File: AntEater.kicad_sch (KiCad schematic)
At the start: 3 parts, among them CN1 X2026WRS-2X09D-LPSW, CN2 X2026WRS-2X09D-LPSW, J1 Conn_01x10_MountingPin

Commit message: placed and routed
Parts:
- removed J1: Conn_01x10_MountingPin, Connector_PinHeader_2.54mm:PinHeader_1x11_P2.54mm_Vertical, symbol Connector_Generic:Conn_01x11
- added C1, C11, C12, C13, C14, C3, C5, C8, C9: 0.1uF, Capacitor_SMD:C_0805_2012Metric, symbol Device:C
- added C10: 3.3uF, Capacitor_SMD:C_0805_2012Metric, symbol Device:C
- added C2, C7: 27pf, Capacitor_SMD:C_0805_2012Metric, symbol Device:C
- added C4, C6: 4.7uF, Capacitor_SMD:C_1206_3216Metric, symbol Device:C_Polarized
- added FB1, FB2: FerriteBead_Small, Resistor_SMD:R_0603_1608Metric, symbol Device:FerriteBead_Small
- added J2: USB_C_Receptacle_USB2.0, Connector_USB:USB_C_Receptacle_GCT_USB4105-xx-A_16P_TopMnt_Horizontal, symbol Connector:USB_C_Receptacle_USB2.0
- added J3: Conn_02x06_Odd_Even, Connector_PinHeader_2.54mm:PinHeader_2x06_P2.54mm_Vertical, symbol Connector_Generic:Conn_02x06_Odd_Even
- added JP1, JP2: SolderJumper_2_Open, Jumper:SolderJumper-2_P1.3mm_Open_RoundedPad1.0x1.5mm, symbol Jumper:SolderJumper_2_Open
- added R1: 2.2K, Resistor_SMD:R_0805_2012Metric, symbol Device:R_US
- added R2, R3, R4: 10K, Resistor_SMD:R_0805_2012Metric, symbol Device:R_US
- added R5, R7: 5.1K, Resistor_SMD:R_0805_2012Metric, symbol Device:R_US
- added R6: 12K, Resistor_SMD:R_0805_2012Metric, symbol Device:R_US
- added R8: 1K, Resistor_SMD:R_0805_2012Metric, symbol Device:R_US
- added U1: M93C46-WDW6TP, bitcrane:TSSOP8_STM, symbol bitcrane:M93C46-WDW6TP
- added U2: FT4232HQ, bitcrane:QFN50P900X900X105-65N, symbol bitcrane:FT4232HQ-REEL
- added Y1: 12MHz, bitcrane:XTAL_405C35B12M00000, symbol bitcrane:405C35B12M00000
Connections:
- net A0: now also J3.10 (Pin_10)
- net A1: now also J3.5 (Pin_5)
- net A2: now also J3.1 (Pin_1)
- net GND: now also C1.2, C10.2, C11.2, C12.2, C13.2, C14.2, C2.2, C3.2, C4.2, C5.2, C6.2, C7.2, C8.2, C9.2, J2.A1 (GND), J2.A12 (GND), J2.B1 (GND), J2.B12 (GND), J2.S1 (SHIELD), J3.11 (Pin_11), J3.12 (Pin_12), R5.1, R6.1, R7.1, U1.5 (VSS), U1.7 (DU), U2.1 (GND), U2.10 (AGND), U2.11 (GND), U2.13 (TEST), U2.15 (GND), U2.25 (GND), U2.35 (GND), U2.47 (GND), U2.5 (GND), U2.51 (GND), U2.65 (EPAD), Y1.2 (GND), Y1.4 (GND__1)
- net PLUG: now also J3.4 (Pin_4)
- net RST: now also J3.7 (Pin_7)
- net RX: now also J3.9 (Pin_9), JP2.2 (B), U2.39 (CDBUS1)
- net SCL: now also J3.2 (Pin_2), U2.16 (ADBUS0)
- net SDA: now also J3.3 (Pin_3), U2.17 (ADBUS1), U2.18 (ADBUS2)
- net TX: now also J3.6 (Pin_6), JP1.2 (B), U2.27 (BDBUS1)
- net 3V3 renamed VCCIO
- net VCCIO: now also C11.1, C13.1, C14.1, C8.1, FB1.1, FB2.1, J3.8 (Pin_8), R2.2, R3.2, R4.2, R8.1, U1.6 (ORG), U1.8 (VCC), U2.20 (VCCIO), U2.31 (VCCIO), U2.42 (VCCIO), U2.50 (VREGIN), U2.56 (VCCIO)
- new net: C12.1, C4.1, FB1.2, U2.4 (VPHY)
- new net: JP2.1 (A), U2.26 (BDBUS0)
- new net: R1.1, U1.3 (D), U2.61 (EEDATA)
- new net: R1.2, R2.1, U1.4 (Q)
- new net: C2.1, U2.2 (OSCI), Y1.1
- new net: C7.1, U2.3 (OSCO), Y1.3
- new net: R4.1, U1.2 (CLK), U2.62 (EECLK)
- new net: C6.1, C9.1, FB2.2, U2.9 (VPLL)
- new net: R3.1, U1.1 (CS), U2.63 (EECS)
- new net: R8.2, U2.14 (RESET#)
- new net: JP1.1 (A), U2.38 (CDBUS0)
- new net: R6.2, U2.6 (REF)
- new net: J2.A7 (D-), J2.B7 (D-), U2.7 (DM)
- new net: J2.A6 (D+), J2.B6 (D+), U2.8 (DP)
- new net: J2.A5 (CC1), R7.2
- new net: J2.B5 (CC2), R5.2
- new net 5V: J2.A4 (VBUS), J2.A9 (VBUS), J2.B4 (VBUS), J2.B9 (VBUS)
- new net VCORE: C1.1, C10.1, C3.1, C5.1, U2.12 (VCORE), U2.37 (VCORE), U2.49 (VREGOUT), U2.64 (VCORE)
- no-connect marks 4 -> 33
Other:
- note added: "RXD"
- note added: "TXD"
- moved on the sheet: CN2

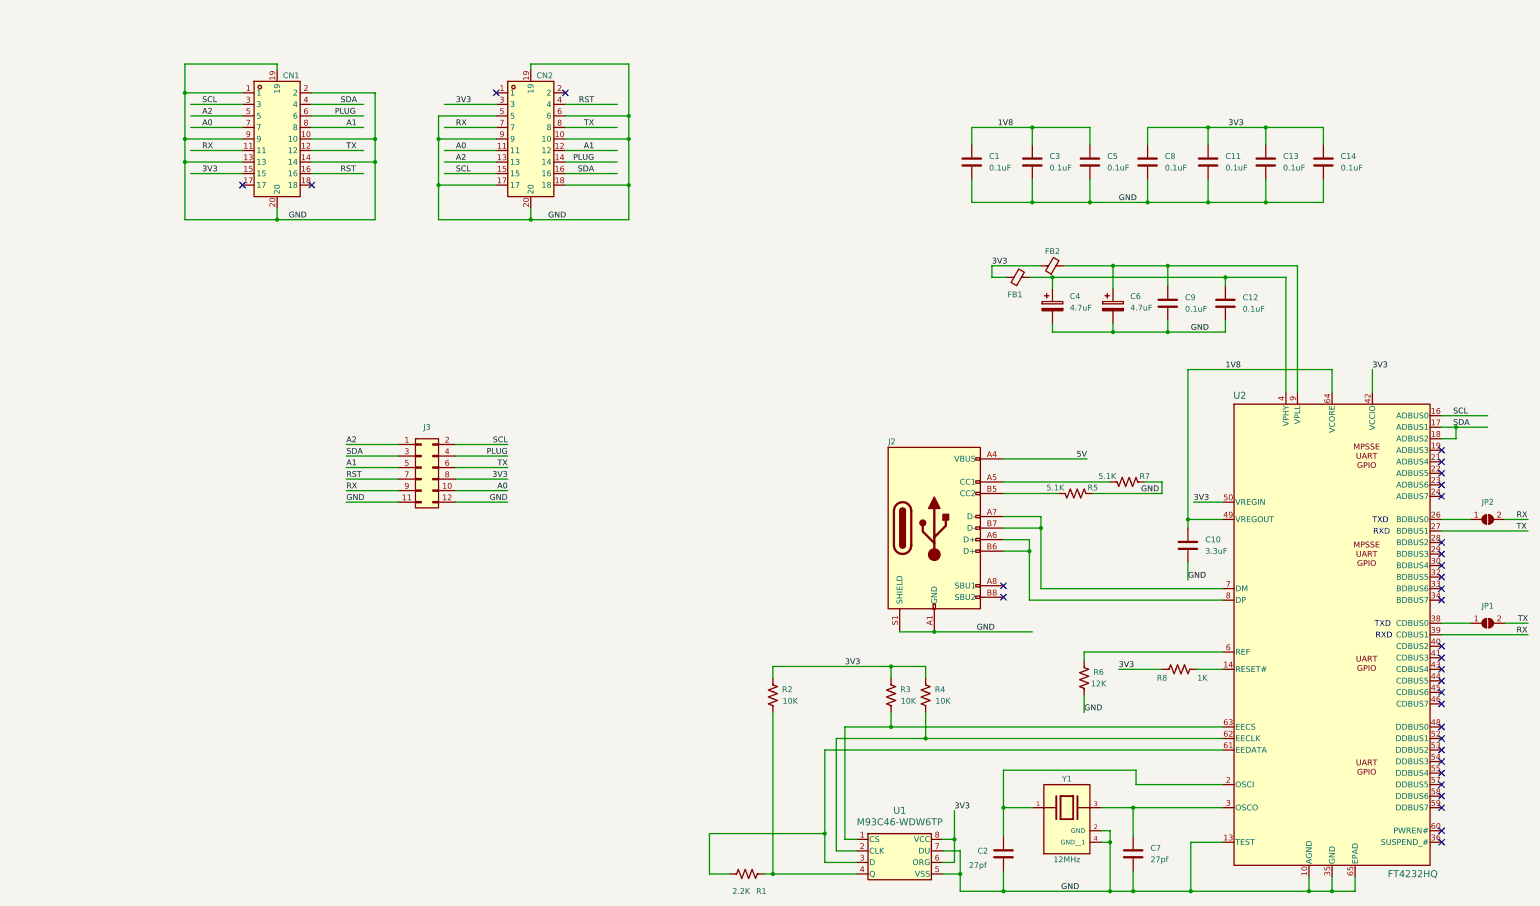
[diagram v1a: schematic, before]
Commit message: added an optional voltage regulator. DRC passed. generated gerbers
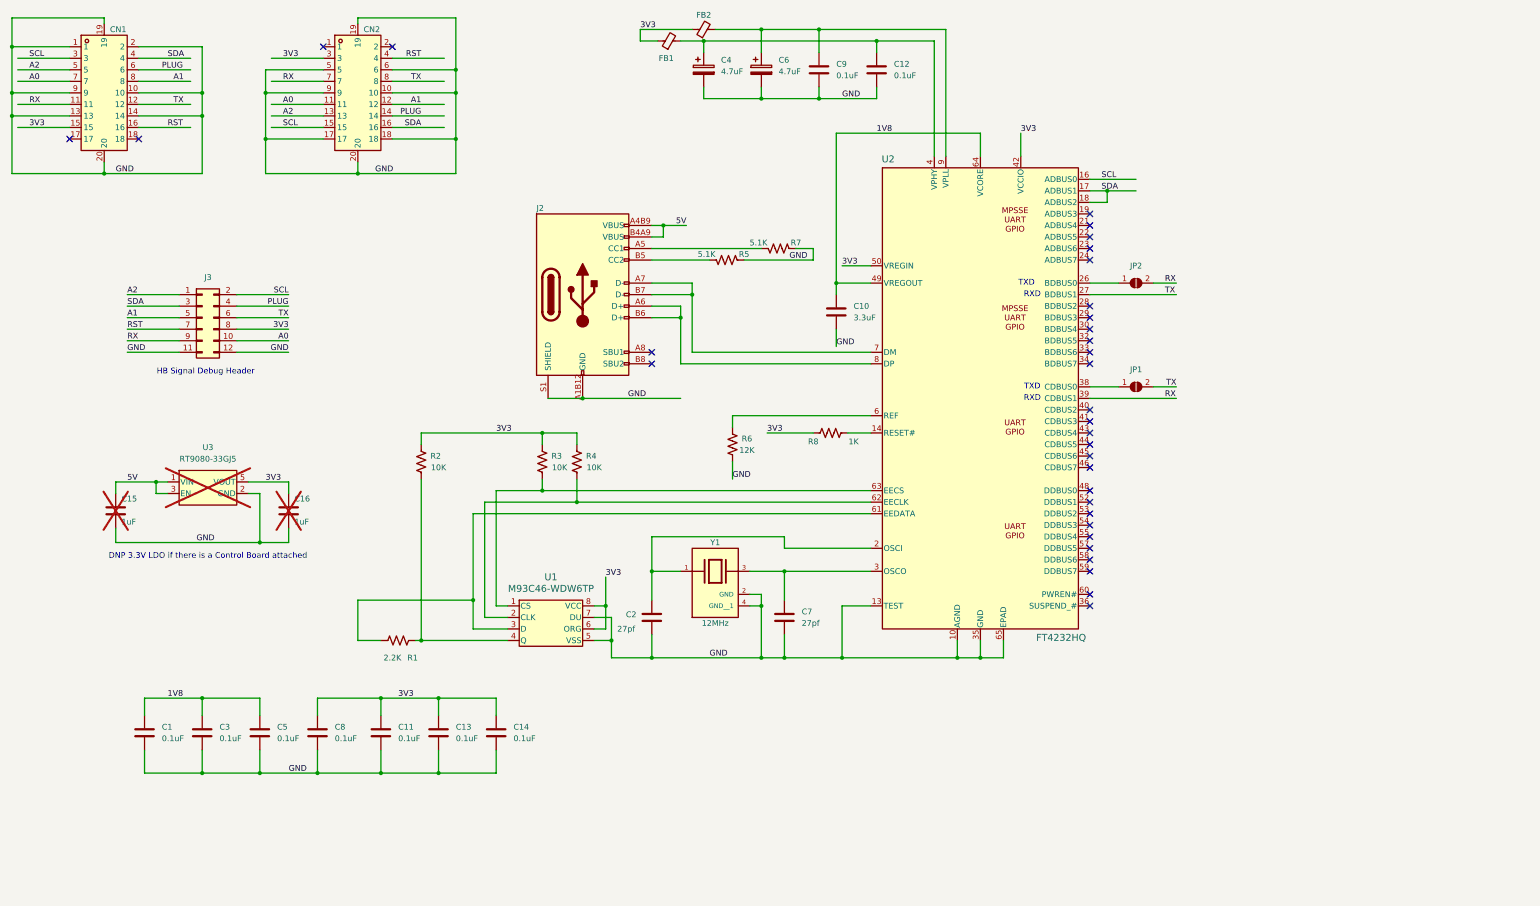
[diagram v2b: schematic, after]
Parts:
- removed J2: USB_C_Receptacle_USB2.0, Connector_USB:USB_C_Receptacle_GCT_USB4105-xx-A_16P_TopMnt_Horizontal, symbol Connector:USB_C_Receptacle_USB2.0
- added C15, C16: 1uF, Capacitor_SMD:C_0805_2012Metric, symbol Device:C
- added J2: USB_C_Receptacle_USB2.0, antsniffer:USB_C_Receptacle_GCT_USB4105-xx-A_16P_TopMnt_Horizontal, symbol antsniffer:USB_C_Receptacle_USB2.0
- added U3: RT9080-33GJ5, antsniffer:RT9080-33GJ5, symbol antsniffer:RT9080-33GJ5
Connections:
- net 5V: now also C15.1, J2.A4B9 (VBUS), J2.B4A9 (VBUS), U3.1 (VIN), U3.3 (EN)
- net GND: now also C15.2, C16.2, J2.A1B12 (GND), J2.B1A12 (GND), J2.S1 (SHIELD), U3.2 (GND)
- net VCCIO: now also C16.1, U3.5 (VOUT)
- net at U2.7 (DM): now also J2.A7 (D-), J2.B7 (D-)
- net at U2.8 (DP): now also J2.A6 (D+), J2.B6 (D+)
- net at R7.2: now also J2.A5 (CC1)
- net at R5.2: now also J2.B5 (CC2)
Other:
- note added: "DNP 3.3V LDO if there is a Control Board attached"
- note added: "HB Signal Debug Header"
- moved on the sheet: C1, C10, C11, C12, C13, C14, C2, C3, C4, C5, C6, C7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

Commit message: switched schematic to RP2040
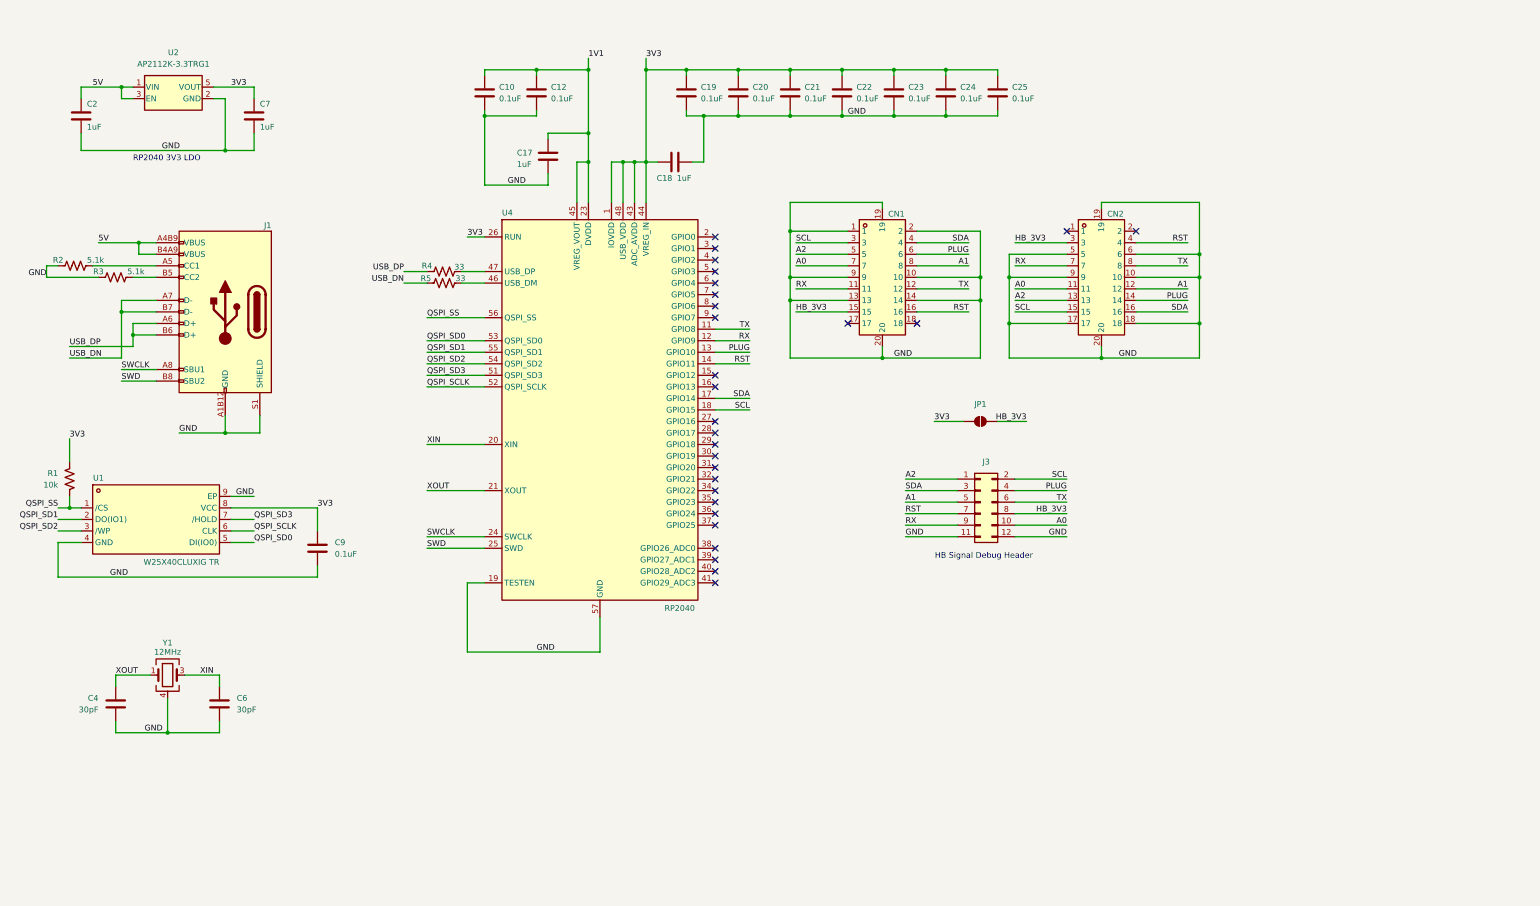
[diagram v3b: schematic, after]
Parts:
- removed C1, C11, C13, C14, C3, C5, C8: 0.1uF, Capacitor_SMD:C_0805_2012Metric, symbol Device:C
- removed C15, C16: 1uF, Capacitor_SMD:C_0805_2012Metric, symbol Device:C
- removed C4, C6: 4.7uF, Capacitor_SMD:C_1206_3216Metric, symbol Device:C_Polarized
- removed FB1, FB2: FerriteBead_Small, Resistor_SMD:R_0603_1608Metric, symbol Device:FerriteBead_Small
- removed J2: USB_C_Receptacle_USB2.0, antsniffer:USB_C_Receptacle_GCT_USB4105-xx-A_16P_TopMnt_Horizontal, symbol antsniffer:USB_C_Receptacle_USB2.0
- removed JP2: SolderJumper_2_Open, Jumper:SolderJumper-2_P1.3mm_Open_RoundedPad1.0x1.5mm, symbol Jumper:SolderJumper_2_Open
- removed R6: 12K, Resistor_SMD:R_0805_2012Metric, symbol Device:R_US
- removed R7: 5.1K, Resistor_SMD:R_0805_2012Metric, symbol Device:R_US
- removed R8: 1K, Resistor_SMD:R_0805_2012Metric, symbol Device:R_US
- removed U1: M93C46-WDW6TP, bitcrane:TSSOP8_STM, symbol bitcrane:M93C46-WDW6TP
- removed U2: FT4232HQ, bitcrane:QFN50P900X900X105-65N, symbol bitcrane:FT4232HQ-REEL
- removed U3: RT9080-33GJ5, antsniffer:RT9080-33GJ5, symbol antsniffer:RT9080-33GJ5
- removed Y1: 12MHz, bitcrane:XTAL_405C35B12M00000, symbol bitcrane:405C35B12M00000
- added C17, C18: 1uF, Capacitor_SMD:C_0402_1005Metric, symbol Device:C
- added C19, C20, C21, C22, C23, C24, C25: 0.1uF, Capacitor_SMD:C_0402_1005Metric, symbol Device:C
- added C4, C6: 30pF, Capacitor_SMD:C_0402_1005Metric, symbol Device:C
- added J1: USB_C_Receptacle_USB2.0, antsniffer:USB_C_Receptacle_GCT_USB4105-xx-A_16P_TopMnt_Horizontal, symbol antsniffer:USB_C_Receptacle_USB2.0
- added U1: W25X40CLUXIG TR, antsniffer:USON8_L2.0-W3.0-P0.50-BL-EP, symbol antsniffer:W25X40CLUXIGTR
- added U2: AP2112K-3.3TRG1, antsniffer:SOT-25-5_L2.9-W1.6-P0.95-LS2.8-BL, symbol antsniffer:AP2112K-3.3TRG1
- added U4: RP2040, Package_DFN_QFN:QFN-56-1EP_7x7mm_P0.4mm_EP3.2x3.2mm, symbol aditBoard:RP2040
- added Y1: 12MHz, antsniffer:OSC-SMD_4P-L3.2-W2.5-BL, symbol Device:Crystal_GND24_common
- C10: value 3.3uF -> 0.1uF; footprint Capacitor_SMD:C_0805_2012Metric -> Capacitor_SMD:C_0402_1005Metric; DK 1276-2912-1-ND -> (none); JLC Part (none) -> Basic Part; LCSC Part (none) -> C307331; Manufacturer (none) -> SAMSUNG(三星); PARTNO CL21A335KPFNNNE -> CL05B104KB54PNC
- C12, C9: footprint Capacitor_SMD:C_0805_2012Metric -> Capacitor_SMD:C_0402_1005Metric; DK 1276-6840-1-ND -> (none); JLC Part (none) -> Basic Part; LCSC Part (none) -> C307331; Manufacturer (none) -> SAMSUNG(三星); PARTNO CL21B104KCFNNNE -> CL05B104KB54PNC
- C2, C7: value 27pf -> 1uF; footprint Capacitor_SMD:C_0805_2012Metric -> Capacitor_SMD:C_0402_1005Metric; DK 1276-2622-1-ND -> 587-5514-1-ND; LCSC Part (none) -> C52923; PARTNO CL21C270JCANNNC -> EMK105BJ105MV-F
- R1: value 2.2K -> 10k; footprint Resistor_SMD:R_0805_2012Metric -> Resistor_SMD:R_0402_1005Metric; DK RMCF0805FT2K20CT-ND -> (none); LCSC Part (none) -> C25744; PARTNO RMCF0805FT2K20 -> (none)
- R2, R3: value 10K -> 5.1k; footprint Resistor_SMD:R_0805_2012Metric -> Resistor_SMD:R_0402_1005Metric; DK RMCF0805FT10K0CT-ND -> RMCF0402JT5K10CT-ND; LCSC Part (none) -> C25905; PARTNO RMCF0805FT10K0 -> RMCF0402JT5K10
- R4: value 10K -> 33; footprint Resistor_SMD:R_0805_2012Metric -> Resistor_SMD:R_0402_1005Metric; DK RMCF0805FT10K0CT-ND -> (none); JLC Part (none) -> Basic Part; LCSC Part (none) -> C25105; Manufacturer (none) -> UNI-ROYAL(厚声); PARTNO RMCF0805FT10K0 -> 0402WGF330JTCE
- R5: value 5.1K -> 33; footprint Resistor_SMD:R_0805_2012Metric -> Resistor_SMD:R_0402_1005Metric; DK 311-5.10KCRCT-ND -> (none); JLC Part (none) -> Basic Part; LCSC Part (none) -> C25105; Manufacturer (none) -> UNI-ROYAL(厚声); PARTNO RC0805FR-075K1L -> 0402WGF330JTCE
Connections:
- net VCORE is gone; now on net GND: C10.1
- net 5V: now also C2.1, J1.A4B9 (VBUS), J1.B4A9 (VBUS), U2.1 (VIN), U2.3 (EN)
- net GND: now also C12.1, C9.1, R2.1, R3.1, C17.1, C18.2, C19.1, C20.1, C21.1, C22.1, C23.1, C24.1, C25.1, C4.1, C6.1, J1.A1B12 (GND), J1.B1A12 (GND), J1.S1 (SHIELD), U1.4 (GND), U1.9 (EP), U2.2 (GND), U4.19 (TESTEN), U4.57 (GND), Y1.2, Y1.4; no longer C10.2, C12.2, C9.2, R5.1
- net PLUG: now also U4.13 (GPIO10)
- net RST: now also U4.14 (GPIO11)
- net RX: now also U4.12 (GPIO9)
- net SCL: now also U4.18 (GPIO15)
- net SDA: now also U4.17 (GPIO14)
- net TX: now also U4.11 (GPIO8); no longer JP1.2 (B)
- net at R5.2: now also U4.46 (USB_DM)
- net 3V3: now reaches R1.1
- net 3V3: now also C7.1, C9.2, JP1.1 (A), C18.1, C19.2, C20.2, C21.2, C22.2, C23.2, C24.2, C25.2, U1.8 (VCC), U2.5 (VOUT), U4.1 (IOVDD), U4.10 (IOVDD), U4.22 (IOVDD), U4.26 (RUN), U4.33 (IOVDD), U4.42 (IOVDD), U4.43 (ADC_AVDD), U4.44 (VREG_IN), U4.48 (USB_VDD), U4.49 (IOVDD)
- net QSPI_SS: now reaches R1.2
- net QSPI_SS: now also U1.1 (/CS), U4.56 (QSPI_SS); no longer R2.1
- net USB_DP: now reaches R4.1
- net USB_DP: now also J1.A6 (D+), J1.B6 (D+)
- net VCCIO renamed HB_3V3
- net HB_3V3: now also JP1.2 (B); no longer R2.2, R3.2, R4.2
- new net: J1.B5 (CC2), R3.2
- new net: J1.A5 (CC1), R2.2
- new net: R4.2, U4.47 (USB_DP)
- new net 1V1: C10.2, C12.2, C17.2, U4.23 (DVDD), U4.45 (VREG_VOUT), U4.50 (DVDD)
- new net QSPI_SCLK: U1.6 (CLK), U4.52 (QSPI_SCLK)
- new net QSPI_SD0: U1.5 (DI(IO0)), U4.53 (QSPI_SD0)
- new net QSPI_SD1: U1.2 (DO(IO1)), U4.55 (QSPI_SD1)
- new net QSPI_SD2: U1.3 (/WP), U4.54 (QSPI_SD2)
- new net QSPI_SD3: U1.7 (/HOLD), U4.51 (QSPI_SD3)
- new net SWCLK: J1.A8 (SBU1), U4.24 (SWCLK)
- new net SWD: J1.B8 (SBU2), U4.25 (SWD)
- new net USB_DN: J1.A7 (D-), J1.B7 (D-), R5.1
- new net XIN: C6.2, U4.20 (XIN), Y1.3
- new net XOUT: C4.2, U4.21 (XOUT), Y1.1
- no-connect marks 33 -> 28
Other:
- note added: "RP2040 3V3 LDO"
- note removed: "DNP 3.3V LDO if there is a Control Board attached"
- note removed: "RXD"
- note removed: "TXD"
- title: Antsniffer -> AntEater
- moved on the sheet: CN1, CN2, J3
